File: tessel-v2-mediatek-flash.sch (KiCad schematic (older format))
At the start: 8 parts, among them J401 CONN_01X01, J402 CONN_01X01, U401 S25FL256SAGNFI001

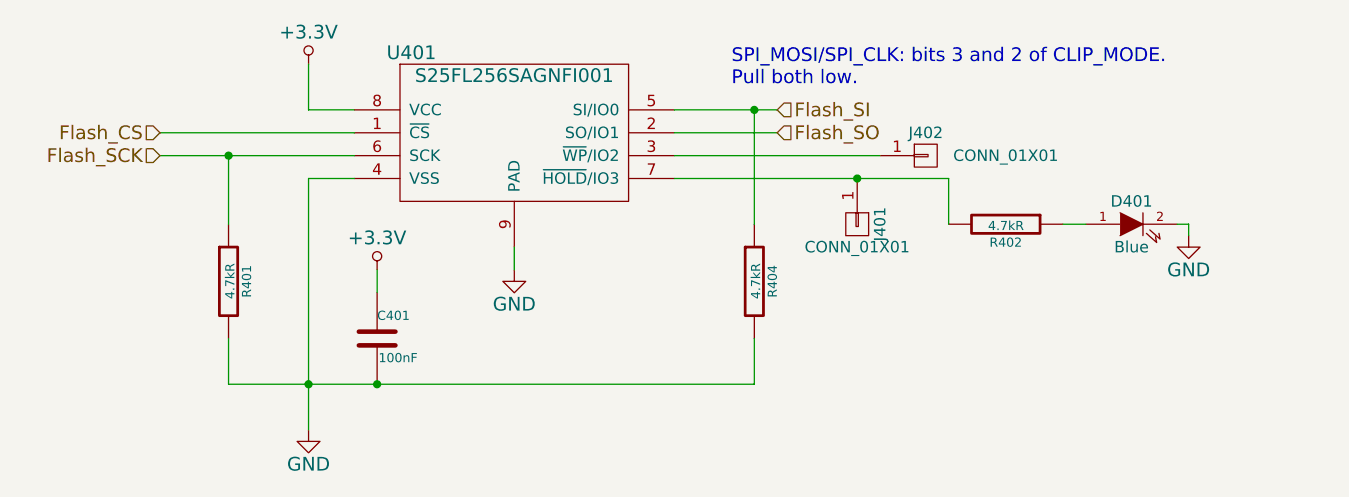
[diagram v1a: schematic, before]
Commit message: apologies jia... needed to re-number things
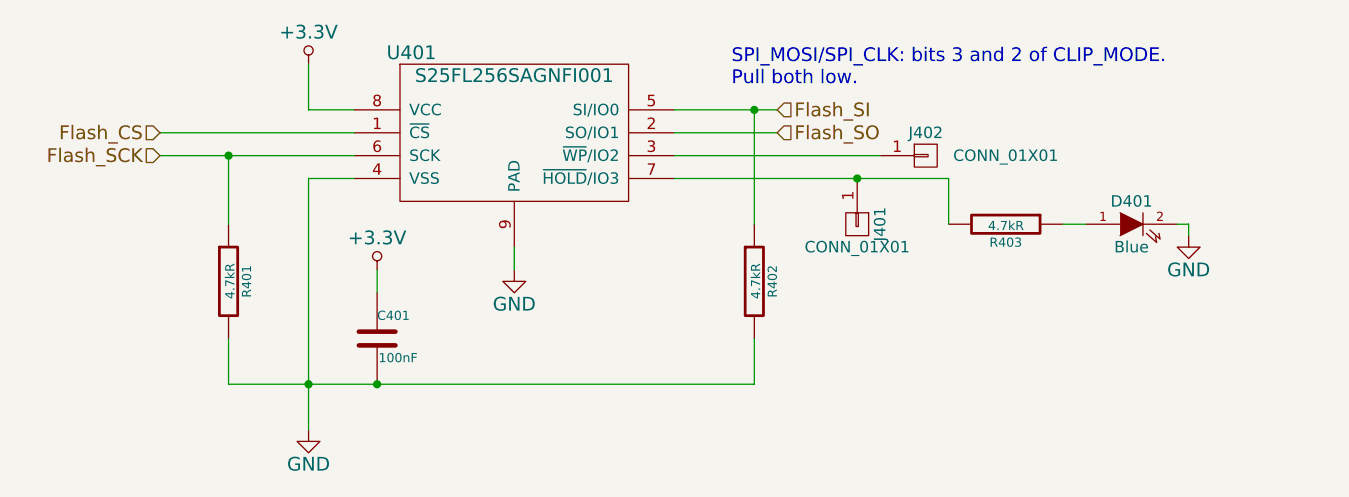
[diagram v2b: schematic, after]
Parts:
- renumbered R404 to R402, R402 to R403
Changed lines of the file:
@@
 Flash_SCK
 $Comp
-L GND #PWR25
+L GND #PWR402
 U 1 1 548FCCD4
 P 6900 5650
-F 0 "#PWR25" H 6900 5400 60  0001 C CNN
+F 0 "#PWR402" H 6900 5400 60  0001 C CNN
 F 1 "GND" H 6900 5500 60  0000 C CNN
 F 2 "" H 6900 5650 60  0000 C CNN
@@
 $EndComp
 $Comp
-L +3.3V #PWR24
+L +3.3V #PWR401
 U 1 1 548FCD0C
 P 6900 4050
-F 0 "#PWR24" H 6900 3900 60  0001 C CNN
+F 0 "#PWR401" H 6900 3900 60  0001 C CNN
 F 1 "+3.3V" H 6900 4190 60  0000 C CNN
 F 2 "" H 6900 4050 60  0000 C CNN
@@
 $EndComp
 $Comp
-L +3.3V #PWR26
+L +3.3V #PWR403
 U 1 1 548FCD90
 P 7200 4950
-F 0 "#PWR26" H 7200 4800 60  0001 C CNN
+F 0 "#PWR403" H 7200 4800 60  0001 C CNN
 F 1 "+3.3V" H 7200 5090 60  0000 C CNN
 F 2 "" H 7200 4950 60  0000 C CNN
@@
 	6550 5250 6550 5450
 $Comp
-L R R404
+L R R402
 U 1 1 54923AA1
 P 8850 5000
-F 0 "R404" V 8930 5000 40  0000 C CNN
+F 0 "R402" V 8930 5000 40  0000 C CNN
 F 1 "4.7kR" V 8857 5001 40  0000 C CNN
 F 2 "tm-kicad-lib:SMD-0402" V 8780 5000 30  0001 C CNN
@@
 	8500 4550 9700 4550
 $Comp
-L GND #PWR27
+L GND #PWR404
 U 1 1 5495E6FE
 P 7800 4950
-F 0 "#PWR27" H 7800 4700 60  0001 C CNN
+F 0 "#PWR404" H 7800 4700 60  0001 C CNN
 F 1 "GND" H 7800 4800 60  0000 C CNN
 F 2 "" H 7800 4950 60  0000 C CNN
@@
 $EndComp
 $Comp
-L R R402
+L R R403
 U 1 1 5497E32A
 P 9950 4750
-F 0 "R402" V 10030 4750 40  0000 C CNN
+F 0 "R403" V 10030 4750 40  0000 C CNN
 F 1 "4.7kR" V 9957 4751 40  0000 C CNN
 F 2 "tm-kicad-lib:SMD-0402" V 9880 4750 30  0001 C CNN
@@
 	10200 4750 10300 4750
 $Comp
-L GND #PWR28
+L GND #PWR405
 U 1 1 5497E4CF
 P 10750 4800
-F 0 "#PWR28" H 10750 4550 60  0001 C CNN
+F 0 "#PWR405" H 10750 4550 60  0001 C CNN
 F 1 "GND" H 10750 4650 60  0000 C CNN
 F 2 "" H 10750 4800 60  0000 C CNN

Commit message: swd/jtag pinswaps and LEDs
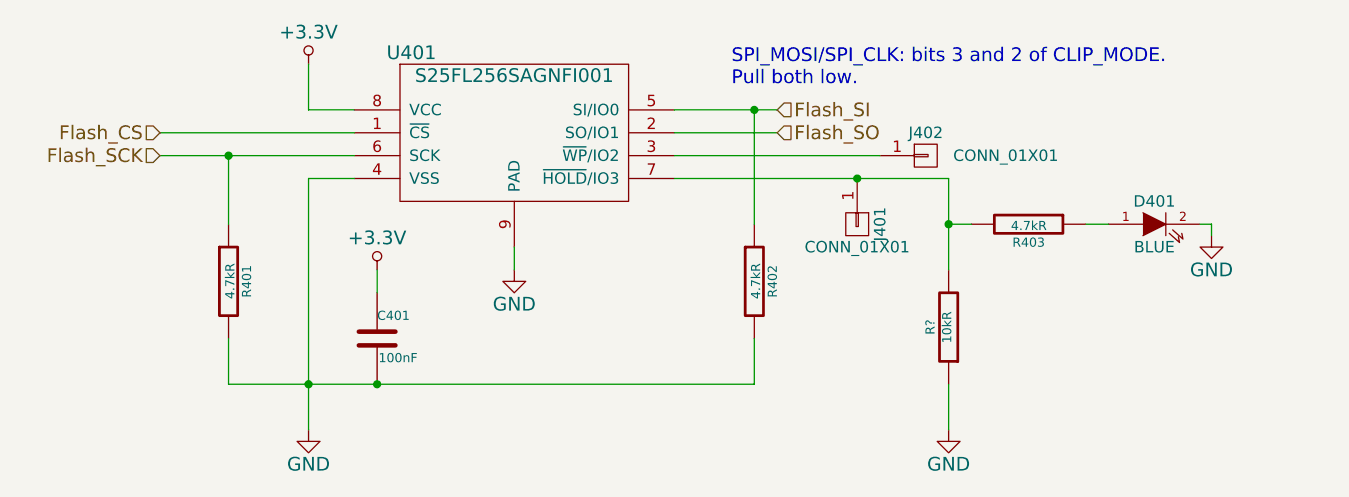
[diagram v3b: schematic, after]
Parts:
- added R?: 10kR, tm-kicad-lib:SMD-0402, symbol R
- D401: value Blue -> BLUE
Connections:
- net GND: now also R?.1
- net at J401.1 (P1), R403.2, U401.7 (~HOLD~/IO3): now also R?.2
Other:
- moved on the sheet: D401, R403
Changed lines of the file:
@@
 	7100 4350 6250 4350
 Wire Wire Line
-	6250 4450 7100 4450
+	6250 4450 6550 4450
+Wire Wire Line
+	6550 4450 7100 4450
 Wire Wire Line
 	7100 4550 6900 4550
 Wire Wire Line
-	8500 4250 8950 4250
+	8500 4250 8850 4250
+Wire Wire Line
+	8850 4250 8950 4250
 Wire Wire Line
 	8500 4350 8950 4350
 Wire Wire Line
-	6900 4550 6900 5650
+	6900 4550 6900 5450
+Wire Wire Line
+	6900 5450 6900 5650
 Wire Wire Line
 	6900 4250 6900 4050
 Wire Wire Line
-	6550 5450 8850 5450
+	6550 5450 6900 5450
+Wire Wire Line
+	6900 5450 7200 5450
+Wire Wire Line
+	7200 5450 8850 5450
 Connection ~ 6900 5450
 Wire Wire Line
@@
 	8500 4450 9400 4450
 Wire Wire Line
-	8500 4550 9700 4550
+	8500 4550 9300 4550
+Wire Wire Line
+	9300 4550 9700 4550
 $Comp
 L GND #PWR404
@@
 L LED D401
 U 1 1 5497E278
-P 10500 4750
-F 0 "D401" H 10500 4850 50  0000 C CNN
-F 1 "Blue" H 10500 4650 50  0000 C CNN
-F 2 "SMD_Packages:SMD-0603" H 10500 4750 60  0001 C CNN
-F 3 "" H 10500 4750 60  0000 C CNN
-	1    10500 4750
+P 10600 4750
+F 0 "D401" H 10600 4850 50  0000 C CNN
+F 1 "BLUE" H 10600 4650 50  0000 C CNN
+F 2 "SMD_Packages:SMD-0603" H 10600 4750 60  0001 C CNN
+F 3 "" H 10600 4750 60  0000 C CNN
+	1    10600 4750
 	1    0    0    -1
 $EndComp
@@
 L R R403
 U 1 1 5497E32A
-P 9950 4750
-F 0 "R403" V 10030 4750 40  0000 C CNN
-F 1 "4.7kR" V 9957 4751 40  0000 C CNN
-F 2 "tm-kicad-lib:SMD-0402" V 9880 4750 30  0001 C CNN
-F 3 "" H 9950 4750 30  0000 C CNN
-	1    9950 4750
+P 10050 4750
+F 0 "R403" V 10130 4750 40  0000 C CNN
+F 1 "4.7kR" V 10057 4751 40  0000 C CNN
+F 2 "tm-kicad-lib:SMD-0402" V 9980 4750 30  0001 C CNN
+F 3 "" H 10050 4750 30  0000 C CNN
+	1    10050 4750
 	0    1    1    0
 $EndComp
 Wire Wire Line
 	9700 4550 9700 4750
+Wire Wire Line
+	9700 4750 9700 4950
 Connection ~ 9300 4550
 Wire Wire Line
-	10200 4750 10300 4750
+	10300 4750 10400 4750
 $Comp
 L GND #PWR405
 U 1 1 5497E4CF
-P 10750 4800
-F 0 "#PWR405" H 10750 4550 60  0001 C CNN
-F 1 "GND" H 10750 4650 60  0000 C CNN
-F 2 "" H 10750 4800 60  0000 C CNN
-F 3 "" H 10750 4800 60  0000 C CNN
-	1    10750 4800
+P 10850 4800
+F 0 "#PWR405" H 10850 4550 60  0001 C CNN
+F 1 "GND" H 10850 4650 60  0000 C CNN
+F 2 "" H 10850 4800 60  0000 C CNN
+F 3 "" H 10850 4800 60  0000 C CNN
+	1    10850 4800
 	1    0    0    -1
 $EndComp
 Wire Wire Line
-	10700 4750 10750 4750
+	10800 4750 10850 4750
 Wire Wire Line
-	10750 4750 10750 4800
+	10850 4750 10850 4800
+$Comp
+L R R?
+U 1 1 54BF3CBB
+P 9700 5200
+F 0 "R?" V 9780 5200 40  0000 C CNN
+F 1 "10kR" V 9707 5201 40  0000 C CNN
+F 2 "tm-kicad-lib:SMD-0402" V 9630 5200 30  0001 C CNN
+F 3 "" H 9700 5200 30  0000 C CNN
+	1    9700 5200
+	-1   0    0    1
+$EndComp
+Wire Wire Line
+	9700 4750 9800 4750
+Connection ~ 9700 4750
+$Comp
+L GND #PWR?
+U 1 1 54BF3D94
+P 9700 5650
+F 0 "#PWR?" H 9700 5400 60  0001 C CNN
+F 1 "GND" H 9700 5500 60  0000 C CNN
+F 2 "" H 9700 5650 60  0000 C CNN
+F 3 "" H 9700 5650 60  0000 C CNN
+	1    9700 5650
+	1    0    0    -1
+$EndComp
+Wire Wire Line
+	9700 5650 9700 5450
 $EndSCHEMATC

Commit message: re-annotate
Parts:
- gave numbers to parts that had none: 1
- renumbered R403 to R404
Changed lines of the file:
@@
 $EndComp
 $Comp
-L R R403
+L R R404
 U 1 1 5497E32A
 P 10050 4750
-F 0 "R403" V 10130 4750 40  0000 C CNN
+F 0 "R404" V 10130 4750 40  0000 C CNN
 F 1 "4.7kR" V 10057 4751 40  0000 C CNN
 F 2 "tm-kicad-lib:SMD-0402" V 9980 4750 30  0001 C CNN
@@
 	10300 4750 10400 4750
 $Comp
-L GND #PWR405
+L GND #PWR406
 U 1 1 5497E4CF
 P 10850 4800
-F 0 "#PWR405" H 10850 4550 60  0001 C CNN
+F 0 "#PWR406" H 10850 4550 60  0001 C CNN
 F 1 "GND" H 10850 4650 60  0000 C CNN
 F 2 "" H 10850 4800 60  0000 C CNN
@@
 	10850 4750 10850 4800
 $Comp
-L R R?
+L R R403
 U 1 1 54BF3CBB
 P 9700 5200
-F 0 "R?" V 9780 5200 40  0000 C CNN
+F 0 "R403" V 9780 5200 40  0000 C CNN
 F 1 "10kR" V 9707 5201 40  0000 C CNN
 F 2 "tm-kicad-lib:SMD-0402" V 9630 5200 30  0001 C CNN
@@
 Connection ~ 9700 4750
 $Comp
-L GND #PWR?
+L GND #PWR405
 U 1 1 54BF3D94
 P 9700 5650
-F 0 "#PWR?" H 9700 5400 60  0001 C CNN
+F 0 "#PWR405" H 9700 5400 60  0001 C CNN
 F 1 "GND" H 9700 5500 60  0000 C CNN
 F 2 "" H 9700 5650 60  0000 C CNN

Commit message: re-re-re-etc. annotate
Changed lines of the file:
@@
 	7100 4350 6250 4350
 Wire Wire Line
-	6250 4450 6550 4450
-Wire Wire Line
-	6550 4450 7100 4450
+	6250 4450 7100 4450
 Wire Wire Line
 	7100 4550 6900 4550
 Wire Wire Line
-	8500 4250 8850 4250
-Wire Wire Line
-	8850 4250 8950 4250
+	8500 4250 8950 4250
 Wire Wire Line
 	8500 4350 8950 4350
 Wire Wire Line
-	6900 4550 6900 5450
-Wire Wire Line
-	6900 5450 6900 5650
+	6900 4550 6900 5650
 Wire Wire Line
 	6900 4250 6900 4050
 Wire Wire Line
-	6550 5450 6900 5450
-Wire Wire Line
-	6900 5450 7200 5450
-Wire Wire Line
-	7200 5450 8850 5450
+	6550 5450 8850 5450
 Connection ~ 6900 5450
 Wire Wire Line
@@
 	8500 4450 9400 4450
 Wire Wire Line
-	8500 4550 9300 4550
-Wire Wire Line
-	9300 4550 9700 4550
+	8500 4550 9700 4550
 $Comp
 L GND #PWR404
@@
 $EndComp
 Wire Wire Line
-	9700 4550 9700 4750
-Wire Wire Line
-	9700 4750 9700 4950
+	9700 4550 9700 4950
 Connection ~ 9300 4550
 Wire Wire Line

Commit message: datasheets, refdes, netlists, and component mappings
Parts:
- D401: footprint SMD_Packages:SMD-0603 -> LEDs:LED-0603
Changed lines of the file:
@@
 F 0 "D401" H 10600 4850 50  0000 C CNN
 F 1 "BLUE" H 10600 4650 50  0000 C CNN
-F 2 "SMD_Packages:SMD-0603" H 10600 4750 60  0001 C CNN
+F 2 "LEDs:LED-0603" H 10600 4750 60  0001 C CNN
 F 3 "" H 10600 4750 60  0000 C CNN
 	1    10600 4750

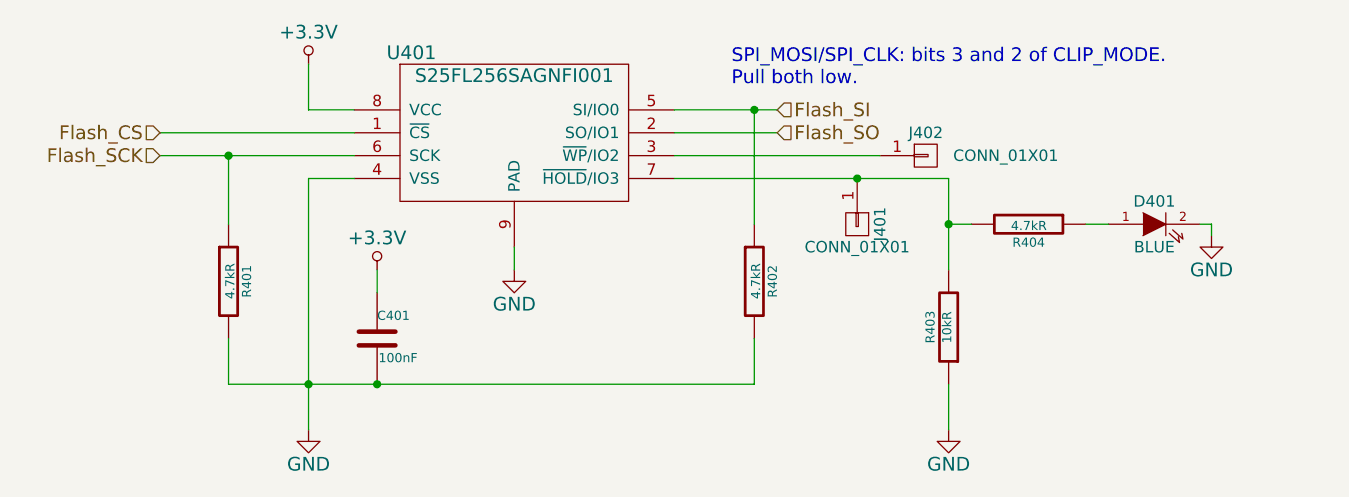
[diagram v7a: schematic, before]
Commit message: usb lines routed
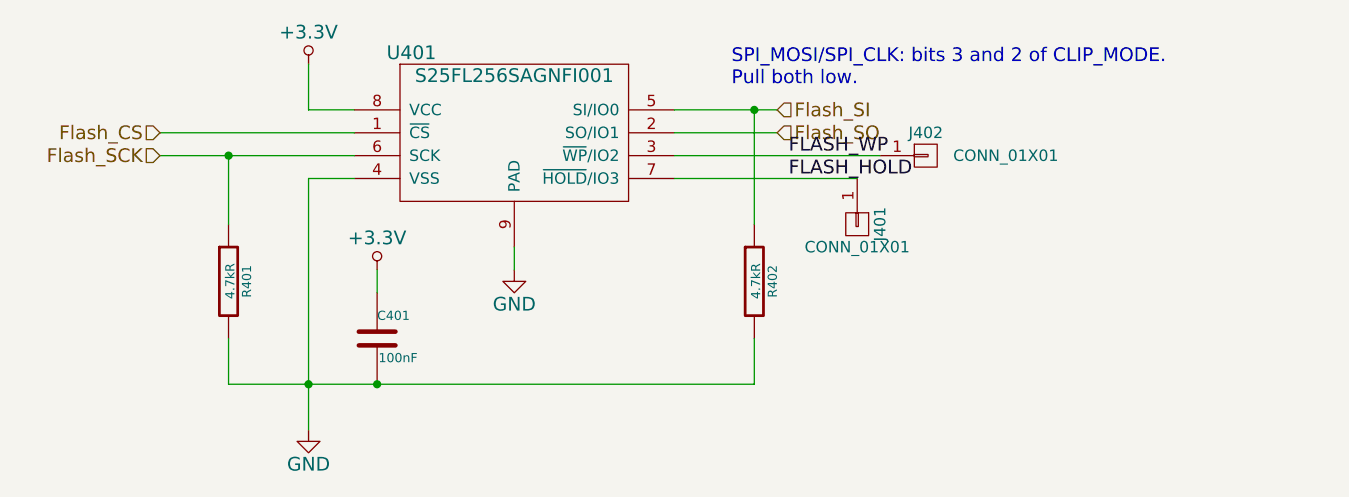
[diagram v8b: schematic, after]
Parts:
- removed D401: BLUE, LEDs:LED-0603, symbol LED
- removed R403: 10kR, tm-kicad-lib:SMD-0402, symbol R
- removed R404: 4.7kR, tm-kicad-lib:SMD-0402, symbol R
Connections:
- net FLASH_WP: now reaches J402.1 (P1), U401.3 (~WP~/IO2)
- net FLASH_HOLD: now reaches J401.1 (P1), U401.7 (~HOLD~/IO3)
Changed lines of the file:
@@
 Wire Wire Line
 	8500 4450 9400 4450
-Wire Wire Line
-	8500 4550 9700 4550
 $Comp
 L GND #PWR028
@@
 Wire Wire Line
 	7800 4950 7800 4850
-$Comp
-L LED D401
-U 1 1 5497E278
-P 10600 4750
-F 0 "D401" H 10600 4850 50  0000 C CNN
-F 1 "BLUE" H 10600 4650 50  0000 C CNN
-F 2 "LEDs:LED-0603" H 10600 4750 60  0001 C CNN
-F 3 "" H 10600 4750 60  0000 C CNN
-	1    10600 4750
-	1    0    0    -1
-$EndComp
-$Comp
-L R R404
-U 1 1 5497E32A
-P 10050 4750
-F 0 "R404" V 10130 4750 40  0000 C CNN
-F 1 "4.7kR" V 10057 4751 40  0000 C CNN
-F 2 "tm-kicad-lib:SMD-0402" V 9980 4750 30  0001 C CNN
-F 3 "" H 10050 4750 30  0000 C CNN
-	1    10050 4750
-	0    1    1    0
-$EndComp
 Wire Wire Line
-	9700 4550 9700 4950
-Connection ~ 9300 4550
-Wire Wire Line
-	10300 4750 10400 4750
-$Comp
-L GND #PWR029
-U 1 1 5497E4CF
-P 10850 4800
-F 0 "#PWR029" H 10850 4550 60  0001 C CNN
-F 1 "GND" H 10850 4650 60  0000 C CNN
-F 2 "" H 10850 4800 60  0000 C CNN
-F 3 "" H 10850 4800 60  0000 C CNN
-	1    10850 4800
-	1    0    0    -1
-$EndComp
-Wire Wire Line
-	10800 4750 10850 4750
-Wire Wire Line
-	10850 4750 10850 4800
-$Comp
-L R R403
-U 1 1 54BF3CBB
-P 9700 5200
-F 0 "R403" V 9780 5200 40  0000 C CNN
-F 1 "10kR" V 9707 5201 40  0000 C CNN
-F 2 "tm-kicad-lib:SMD-0402" V 9630 5200 30  0001 C CNN
-F 3 "" H 9700 5200 30  0000 C CNN
-	1    9700 5200
-	-1   0    0    1
-$EndComp
-Wire Wire Line
-	9700 4750 9800 4750
-Connection ~ 9700 4750
-$Comp
-L GND #PWR030
-U 1 1 54BF3D94
-P 9700 5650
-F 0 "#PWR030" H 9700 5400 60  0001 C CNN
-F 1 "GND" H 9700 5500 60  0000 C CNN
-F 2 "" H 9700 5650 60  0000 C CNN
-F 3 "" H 9700 5650 60  0000 C CNN
-	1    9700 5650
-	1    0    0    -1
-$EndComp
-Wire Wire Line
-	9700 5650 9700 5450
+	8500 4550 9300 4550
+Text Label 9000 4550 0    60   ~ 0
+FLASH_HOLD
+Text Label 9000 4450 0    60   ~ 0
+FLASH_WP
 $EndSCHEMATC
